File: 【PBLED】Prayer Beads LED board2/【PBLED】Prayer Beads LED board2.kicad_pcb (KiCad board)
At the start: 2 copper layers, 17.8 x 43.2 mm, 175 parts, among them J1 PinSocket_1x01_Vertical, J10 PinSocket_1x01_Vertical, J11 PinSocket_1x01_Vertical, J12 PinSocket_1x01_Vertical, J13 PinSocket_1x01_Vertical, J14 PinSocket_1x01_Vertical, J15 PinSocket_1x01_Vertical, J16 PinSocket_1x01_Vertical, J17 PinSocket_1x01_Vertical, J18 PinSocket_1x01_Vertical, J19 PinSocket_1x01_Vertical, J2 PinSocket_1x01_Vertical, J20 PinSocket_1x01_Vertical, J21 PinSocket_1x01_Vertical, J22 PinSocket_1x01_Vertical, J23 PinSocket_1x01_Vertical, J24 PinSocket_1x01_Vertical, J25 PinSocket_1x01_Vertical, J26 PinSocket_1x01_Vertical, J27 PinSocket_1x01_Vertical, J28 PinSocket_1x01_Vertical, J29 PinSocket_1x01_Vertical, J3 PinSocket_1x01_Vertical, J30 PinSocket_1x01_Vertical, J31 PinSocket_1x01_Vertical, J32 PinSocket_1x08_Vertical, J33 PinSocket_1x01_Vertical, J34 PinSocket_1x01_Vertical, J35 PinSocket_1x01_Vertical, J36 PinSocket_1x01_Vertical, J37 PinSocket_1x01_Vertical, J38 PinSocket_1x01_Vertical, J39 PinSocket_1x01_Vertical, J4 PinSocket_1x01_Vertical, J40 PinSocket_1x01_Vertical, J41 PinSocket_1x01_Vertical, J42 PinSocket_1x01_Vertical, J43 PinSocket_1x01_Vertical, J44 PinSocket_1x01_Vertical, J45 PinSocket_1x01_Vertical, J46 PinSocket_1x01_Vertical, J47 PinSocket_1x01_Vertical, J48 PinSocket_1x01_Vertical, J49 PinSocket_1x01_Vertical, J5 PinSocket_1x01_Vertical, J50 PinSocket_1x01_Vertical, J51 PinSocket_1x01_Vertical, J52 PinSocket_1x01_Vertical, J53 PinSocket_1x01_Vertical, J54 PinSocket_1x01_Vertical, J55 PinSocket_1x01_Vertical, J56 PinSocket_1x01_Vertical, J57 PinSocket_1x01_Vertical, J58 PinSocket_1x01_Vertical, J59 PinSocket_1x01_Vertical, J6 PinSocket_1x01_Vertical, J60 PinSocket_1x01_Vertical, J61 PinSocket_1x01_Vertical, J62 PinSocket_1x01_Vertical, J63 PinSocket_1x01_Vertical, J64 PinSocket_1x01_Vertical, J65 PinSocket_1x01_Vertical, J7 PinSocket_1x01_Vertical, J8 PinSocket_1x01_Vertical, J9 PinSocket_1x01_Vertical, P1 Digital, P2 Analog, P3 CONN_01X01, P4 CONN_01X01, P5 CONN_01X01, P6 CONN_01X01, Q1 AO3400A, Q2 AO3400A, Q3 AO3400A, Q4 AO3400A, Q5 AO3400A, Q6 AO3400A, Q7 AO3400A, Q8 AO3400A, U1 LOGIC-74HC595D(SOIC16)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

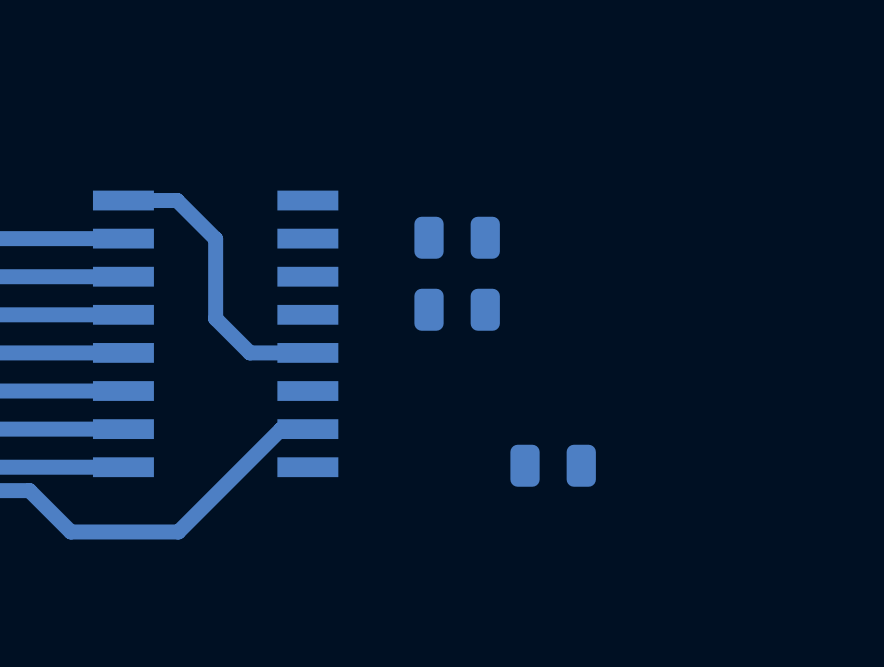
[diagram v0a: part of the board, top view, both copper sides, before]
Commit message: fix u1
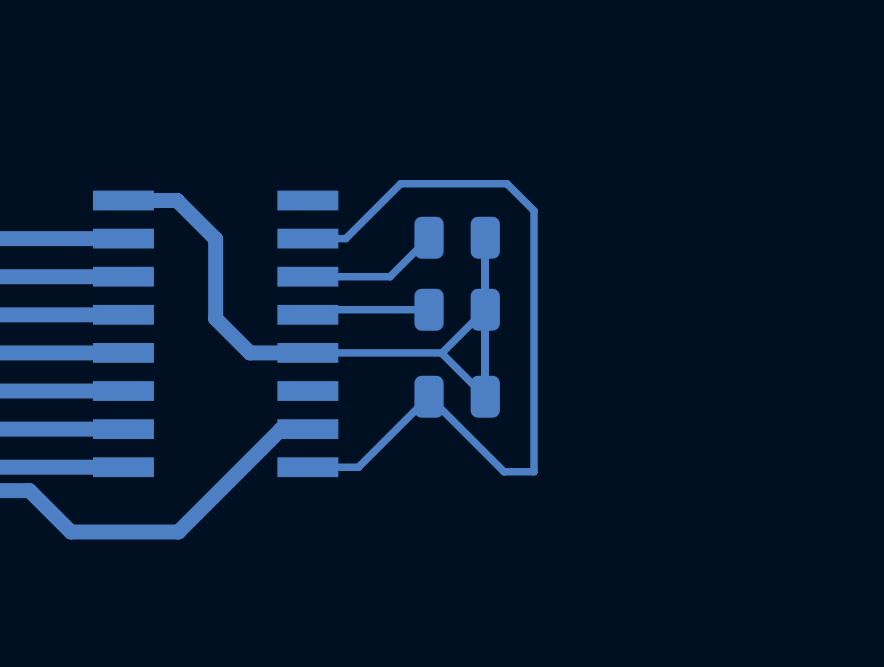
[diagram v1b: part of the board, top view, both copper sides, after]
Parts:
- moved C2 3.94 mm to (204.1, 59.5)
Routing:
- net Net-(C2-Pad2): track 0.00 -> 26.9 mm
- net GND: track 9.81 -> 28.0 mm
- net /3(**): track 0.00 -> 4.58 mm
- net /2: track 0.00 -> 4.11 mm

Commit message: fix 回路図
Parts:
- C10, C11, C12, C16, C17, C18, C22, C23, C24, U4, U6, U8: moved to B.Cu
- moved J32 247.4 mm to (250.5, 19.3), turned to 270 degrees
- moved Q8 243.3 mm to (223.5, 40.5), turned to 90 degrees
- moved Q7 237.7 mm to (228.0, 40.5), turned to 90 degrees
- moved Q6 232.6 mm to (232.5, 40.5), turned to 90 degrees
- moved Q5 227.2 mm to (237.0, 40.5), turned to 90 degrees
- moved Q4 222.2 mm to (241.5, 40.5), turned to 90 degrees
- moved Q3 221.1 mm to (246.0, 40.5), turned to 90 degrees
- moved Q2 219.5 mm to (250.5, 40.5), turned to 90 degrees
- moved Q1 214.9 mm to (255.0, 40.5), turned to 90 degrees
- moved P6 212.1 mm to (210.8, 65.3), turned to 90 degrees
- moved P2 210.0 mm to (213.3, 65.3), turned to 0 degrees
- moved C18 197.6 mm to (181.1, 118.6), turned to 180 degrees
- moved C10 195.8 mm to (181.1, 82.7), turned to 180 degrees
- moved C11 195.3 mm to (181.1, 74.6), turned to 180 degrees
- moved P3 194.8 mm to (210.8, 80.6), turned to 90 degrees
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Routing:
- net GND: track 28.0 -> 521.0 mm
- net Net-(R57-Pad2): track 0.00 -> 156.6 mm
- net Net-(R49-Pad2): track 0.00 -> 155.9 mm
- net Net-(R17-Pad2): track 0.00 -> 155.9 mm
- net Net-(R9-Pad2): track 0.00 -> 155.8 mm
- net Net-(R25-Pad2): track 0.00 -> 155.8 mm
- net Net-(R41-Pad2): track 0.00 -> 155.8 mm
- net Net-(R33-Pad2): track 0.00 -> 155.8 mm
- net Net-(R58-Pad2): track 0.00 -> 129.4 mm
- net Net-(R50-Pad2): track 0.00 -> 128.8 mm
- net Net-(R18-Pad2): track 0.00 -> 128.8 mm
- net Net-(R10-Pad2): track 0.00 -> 128.8 mm
- net Net-(R26-Pad2): track 0.00 -> 128.7 mm
- net Net-(R42-Pad2): track 0.00 -> 128.7 mm
- net Net-(R34-Pad2): track 0.00 -> 128.7 mm
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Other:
- board size 17.8 x 43.2 mm -> 43.2 x 17.8 mm

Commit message: fix
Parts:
- added U9: USB-C, Footprint-library:USB_C, B.Cu at (39.4, 59.5)
- P1, P2, P3, P4, P5, P6: moved to B.Cu
- U1, U2, U3, U4, U5, U6, U7, U8: footprint Footprint-library:SOIC16-1.27-10X3.9MM -> BAYASHI_Footprint-library:SOIC16-1.27-10X3.9MM
- moved Q1 243.3 mm to (32.4, 138.8), turned to 0 degrees
- moved J32 241.1 mm to (37.4, 132.0), turned to 180 degrees
- moved Q2 237.4 mm to (32.4, 134.3), turned to 0 degrees
- moved Q3 231.5 mm to (32.4, 129.8), turned to 0 degrees
- moved P4 228.8 mm to (36.4, 159.0)
- moved P5 228.8 mm to (36.4, 143.7)
- moved Q4 225.6 mm to (32.4, 125.3), turned to 0 degrees
- moved Q5 219.8 mm to (32.4, 120.8), turned to 0 degrees
- moved Q6 214.0 mm to (32.4, 116.3), turned to 0 degrees
- moved Q7 208.2 mm to (32.4, 111.8), turned to 0 degrees
- moved Q8 202.4 mm to (32.4, 107.3), turned to 0 degrees
- moved P1 159.4 mm to (74.5, 159.0), turned to 180 degrees
- moved P2 159.4 mm to (74.5, 143.7), turned to 180 degrees
- moved P3 155.0 mm to (77.0, 159.0)
- moved P6 155.0 mm to (77.0, 143.7)
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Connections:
- C11 pad 2: Net-(C11-Pad2) -> /Vin
- C14 pad 2: Net-(C14-Pad2) -> /Vin
- C17 pad 2: Net-(C17-Pad2) -> /Vin
- C2 pad 2: Net-(C2-Pad2) -> /Vin
- C20 pad 2: Net-(C20-Pad2) -> /Vin
- C23 pad 2: Net-(C23-Pad2) -> /Vin
- C5 pad 2: Net-(C5-Pad2) -> /Vin
- C8 pad 2: Net-(C8-Pad2) -> /Vin
- U1 pad 10: Net-(C2-Pad2) -> /Vin
- U1 pad 16: Net-(C2-Pad2) -> /Vin
- U2 pad 10: Net-(C5-Pad2) -> /Vin
- U2 pad 16: Net-(C5-Pad2) -> /Vin
- U3 pad 10: Net-(C8-Pad2) -> /Vin
- U3 pad 16: Net-(C8-Pad2) -> /Vin
- U4 pad 10: Net-(C11-Pad2) -> /Vin
- U4 pad 16: Net-(C11-Pad2) -> /Vin
- U5 pad 10: Net-(C14-Pad2) -> /Vin
- U5 pad 16: Net-(C14-Pad2) -> /Vin
- U6 pad 10: Net-(C17-Pad2) -> /Vin
- U6 pad 16: Net-(C17-Pad2) -> /Vin
- U7 pad 10: Net-(C20-Pad2) -> /Vin
- U7 pad 16: Net-(C20-Pad2) -> /Vin
- U8 pad 10: Net-(C23-Pad2) -> /Vin
- U8 pad 16: Net-(C23-Pad2) -> /Vin
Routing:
- net /3(**): track 43.2 -> 521.7 mm, vias 0 -> 8
- net /2: track 58.0 -> 281.2 mm, vias 0 -> 8
- net /Vin: track 0.00 -> 213.1 mm
- net GND: track 521.0 -> 613.1 mm
- net Net-(U7-Pad9): track 0.00 -> 31.0 mm, vias 0 -> 2
- net Net-(U3-Pad9): track 0.00 -> 31.0 mm, vias 0 -> 2
- net Net-(U5-Pad9): track 0.00 -> 30.9 mm, vias 0 -> 2
- net Net-(U2-Pad9): track 0.00 -> 30.9 mm, vias 0 -> 2
- net Net-(U4-Pad9): track 0.00 -> 30.9 mm, vias 0 -> 2
- net Net-(U6-Pad9): track 0.00 -> 30.7 mm, vias 0 -> 2
- net Net-(U1-Pad9): track 2.50 -> 30.9 mm, vias 0 -> 2
- net Net-(C14-Pad2): track 27.2 -> 0.00 mm
- net Net-(C5-Pad2): track 27.0 -> 0.00 mm
- net Net-(C8-Pad2): track 26.6 -> 0.00 mm
- net Net-(C23-Pad2): track 26.5 -> 0.00 mm
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- added copper zone on B.Cu, net /2
- added copper zone on B.Cu, net /3(**)
- added copper zone on B.Cu, net GND

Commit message: fix うへへ
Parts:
- added REF**: Jumper_Pad, BAYASHI_Footprint-library:Jumper_Pad, F.Cu at (34.7, 174.4)
- added REF**: Jumper_Pad, BAYASHI_Footprint-library:Jumper_Pad, F.Cu at (214.8, 14.2)
- added REF**: Jumper_Pad, BAYASHI_Footprint-library:Jumper_Pad, F.Cu at (209.8, 174.5)
- added REF**: HIRABAYA, BAYASHI_Footprint-library:HIRABAYA, F.Cu at (36.5, 17.5)
- moved C16 7.35 mm to (206.2, 131.2)
- moved C18 7.35 mm to (206.2, 127.2)
- moved P4 7.35 mm to (42.8, 155.4)
- moved R41 7.35 mm to (47.8, 128.3)
- moved R42 7.35 mm to (67.8, 128.3)
- moved R49 7.35 mm to (47.8, 148.3)
- moved R50 7.35 mm to (67.8, 148.3)
- moved R57 7.35 mm to (47.8, 168.3)
- moved R58 7.35 mm to (67.8, 168.3)
- moved C1 7.35 mm to (206.2, 31.1)
- moved C10 7.35 mm to (206.2, 91.3)
- moved C11 7.35 mm to (206.2, 83.2)
- moved C12 7.35 mm to (206.2, 87.3)
- moved C13 7.35 mm to (206.2, 111.2)
- moved C14 7.35 mm to (206.2, 103.1)
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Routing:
- net /Vin: track 213.1 -> 3096.0 mm, vias 0 -> 1
- net GND: track 613.1 -> 1455.2 mm
- net /4: track 1.70 -> 190.4 mm
- net /3(**): track 521.7 -> 671.6 mm
- net /2: track 281.2 -> 422.9 mm
- net /Reset: track 0.00 -> 72.6 mm
- net /A7: track 0.00 -> 52.2 mm, vias 0 -> 1
- net /A6: track 0.00 -> 49.4 mm, vias 0 -> 1
- net /A5: track 0.00 -> 47.5 mm, vias 0 -> 1
- net /A4: track 0.00 -> 41.6 mm, vias 0 -> 1
- net /A3: track 0.00 -> 35.0 mm, vias 0 -> 1
- net /A2: track 0.00 -> 28.6 mm, vias 0 -> 1
- net /A1: track 0.00 -> 22.4 mm, vias 0 -> 1
- net /A0: track 0.00 -> 17.1 mm, vias 0 -> 1
- added copper zone on B.Cu, net /Vin
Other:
- board size 43.2 x 17.8 mm -> 179.8 x 160.5 mm

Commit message: fix aaa
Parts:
- removed REF** (x3): Jumper_Pad, BAYASHI_Footprint-library:Jumper_Pad
- removed REF**: HIRABAYA, BAYASHI_Footprint-library:HIRABAYA
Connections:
- net +3V3 renamed Net-(P2-Pad14)
- net /13(SCK) renamed Net-(P2-Pad15)
- net /AREF renamed Net-(P2-Pad13)
- C11 pad 2: /Vin -> +5V
- C14 pad 2: /Vin -> +5V
- C17 pad 2: /Vin -> +5V
- C2 pad 2: /Vin -> +5V
- C20 pad 2: /Vin -> +5V
- C23 pad 2: /Vin -> +5V
- C5 pad 2: /Vin -> +5V
- C8 pad 2: /Vin -> +5V
- P2 pad 1: /Vin -> Net-(P2-Pad1)
- U1 pad 10: /Vin -> +5V
- U1 pad 16: /Vin -> +5V
- U2 pad 10: /Vin -> +5V
- U2 pad 16: /Vin -> +5V
- U3 pad 10: /Vin -> +5V
- U3 pad 16: /Vin -> +5V
- U4 pad 10: /Vin -> +5V
- U4 pad 16: /Vin -> +5V
- U5 pad 10: /Vin -> +5V
- U5 pad 16: /Vin -> +5V
- U6 pad 10: /Vin -> +5V
- U6 pad 16: /Vin -> +5V
- U7 pad 10: /Vin -> +5V
- U7 pad 16: /Vin -> +5V
- U8 pad 10: /Vin -> +5V
- U8 pad 16: /Vin -> +5V
- U9 pad A9: /Vin -> +5V
- U9 pad B9: /Vin -> +5V
- U9 pad S2: (no net) -> GND
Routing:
- net /Vin: track 3096.0 -> 0.00 mm, vias 1 -> 0
- net +5V: track 0.00 -> 3041.7 mm, vias 0 -> 3
- net GND: track 1455.2 -> 1499.6 mm
- added copper zone on B.Cu, net +5V
- removed copper zone on B.Cu, net /Vin
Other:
- board size 179.8 x 160.5 mm -> 182.8 x 160.5 mm
